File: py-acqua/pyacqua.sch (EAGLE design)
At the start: 35 parts, among them IC1 uln2308, K1 JS-M1-9V-4, K2 JS-M1-9V-4, K3 JS-M1-9V-4, K4 JS-M1-9V-4, T1 BC547, T2 BC547, X1 MSTBA4

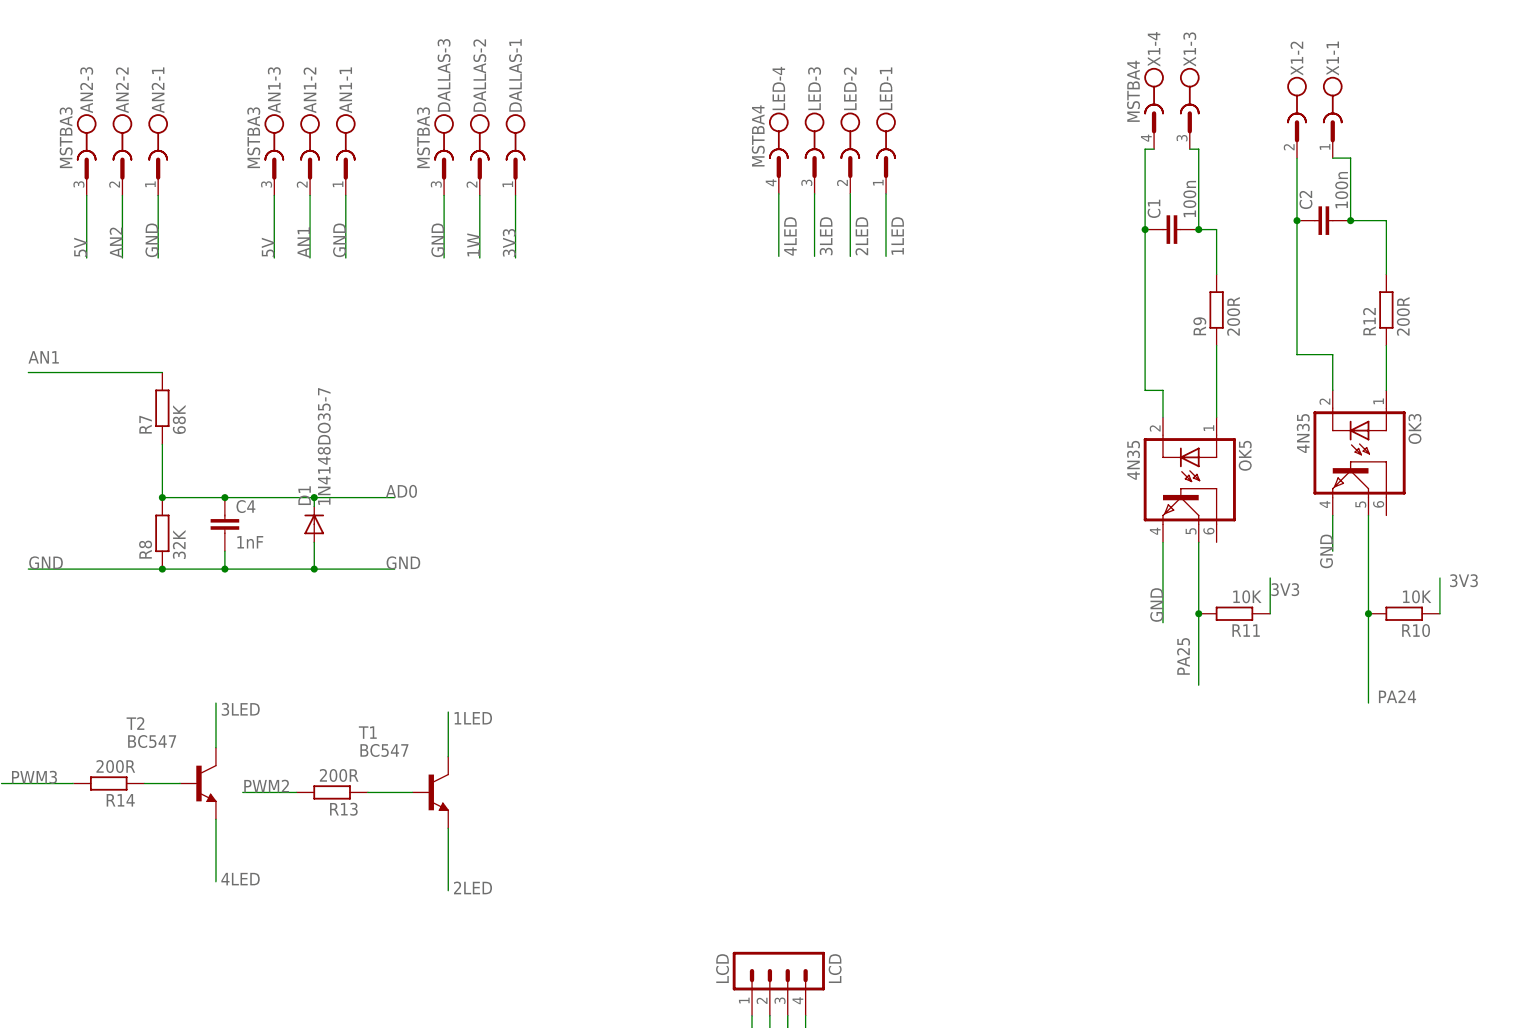
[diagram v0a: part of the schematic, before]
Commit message: sistemazioni input su py-acqua
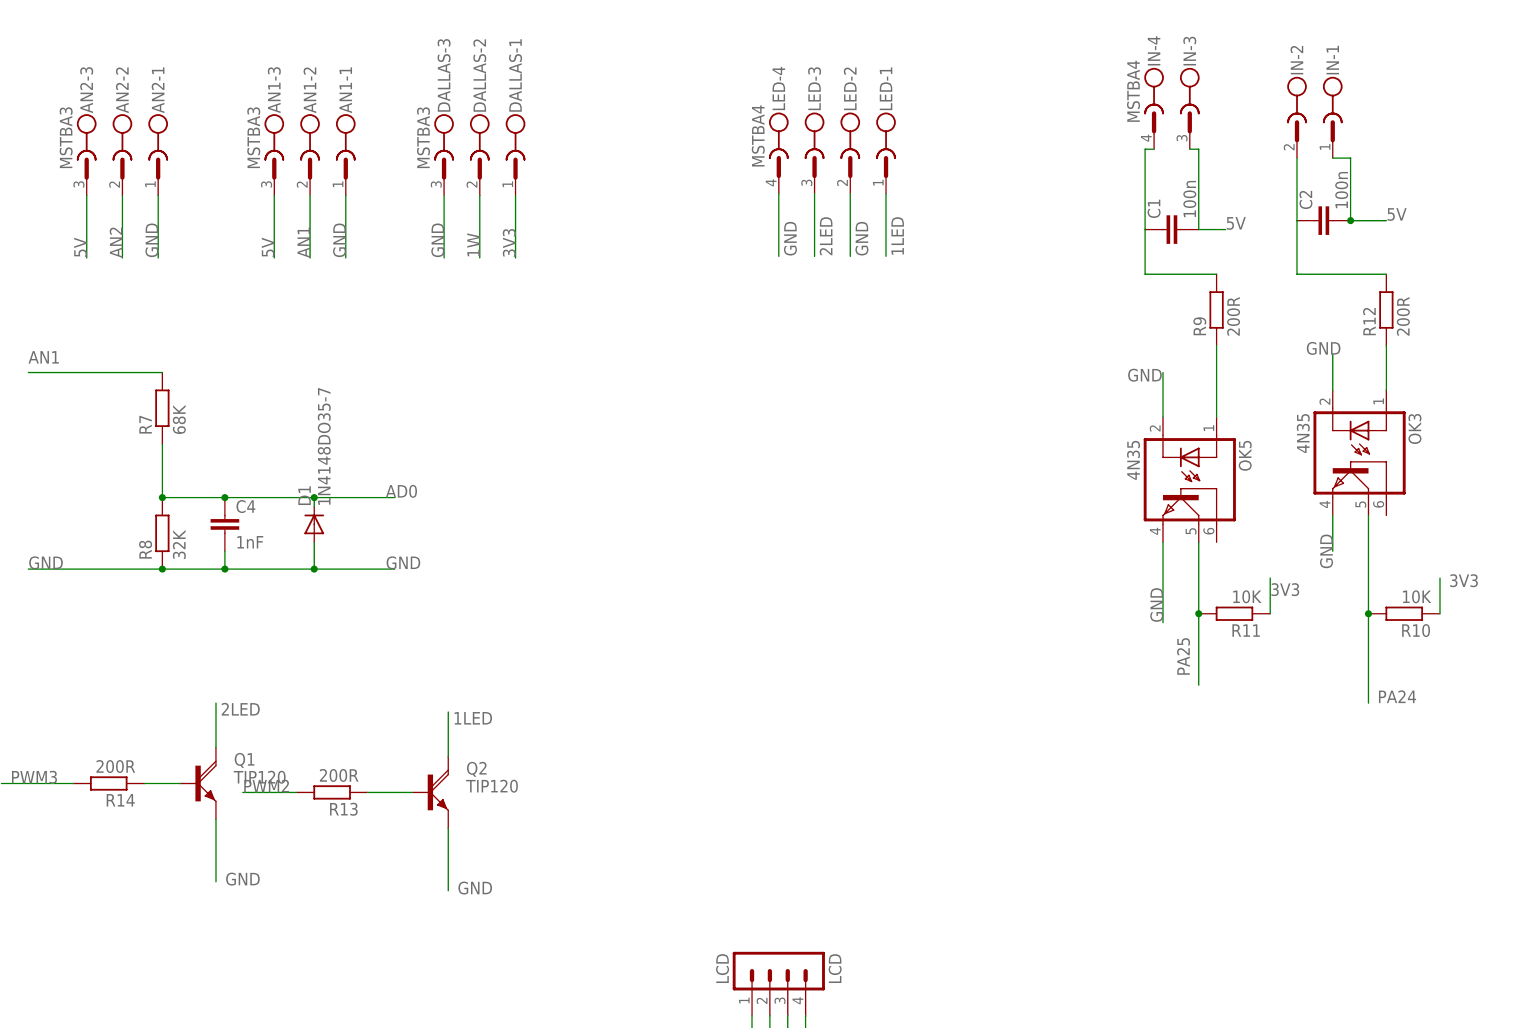
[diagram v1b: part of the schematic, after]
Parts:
- removed T1, T2: BC547, transistor:BC547
- added Q1, Q2: TIP120, transistor-power:TIP120
- renumbered X1 to IN
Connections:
- removed net 3LED: LED-3.1, T2.C
- removed net 4LED: LED-4.1, T2.E
- removed net N$2: C2.2, IN-1.1, R12.2
- removed net N$4: C2.1, IN-2.1, OK3.C
- removed net N$7: C1.2, IN-3.1, R9.2
- new net N$5: C2.1, IN-2.1, R12.2
- net 1LED: now also Q2.C; no longer T1.C
- net 2LED: now also LED-3.1, Q1.C; no longer LED-2.1, T1.E
- net 5V: now also C1.2, C2.2, IN-1.1, IN-3.1
- net GND: now also LED-2.1, LED-4.1, OK3.C, OK5.C, Q1.E, Q2.E
- net N$10: now also R9.2; no longer OK5.C
- net N$11: now also Q1.B; no longer T2.B
- net N$9: now also Q2.B; no longer T1.B
